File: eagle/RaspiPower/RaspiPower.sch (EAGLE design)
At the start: 6 parts, among them J3 455-1750-1-ND, J4 455-1750-1-ND

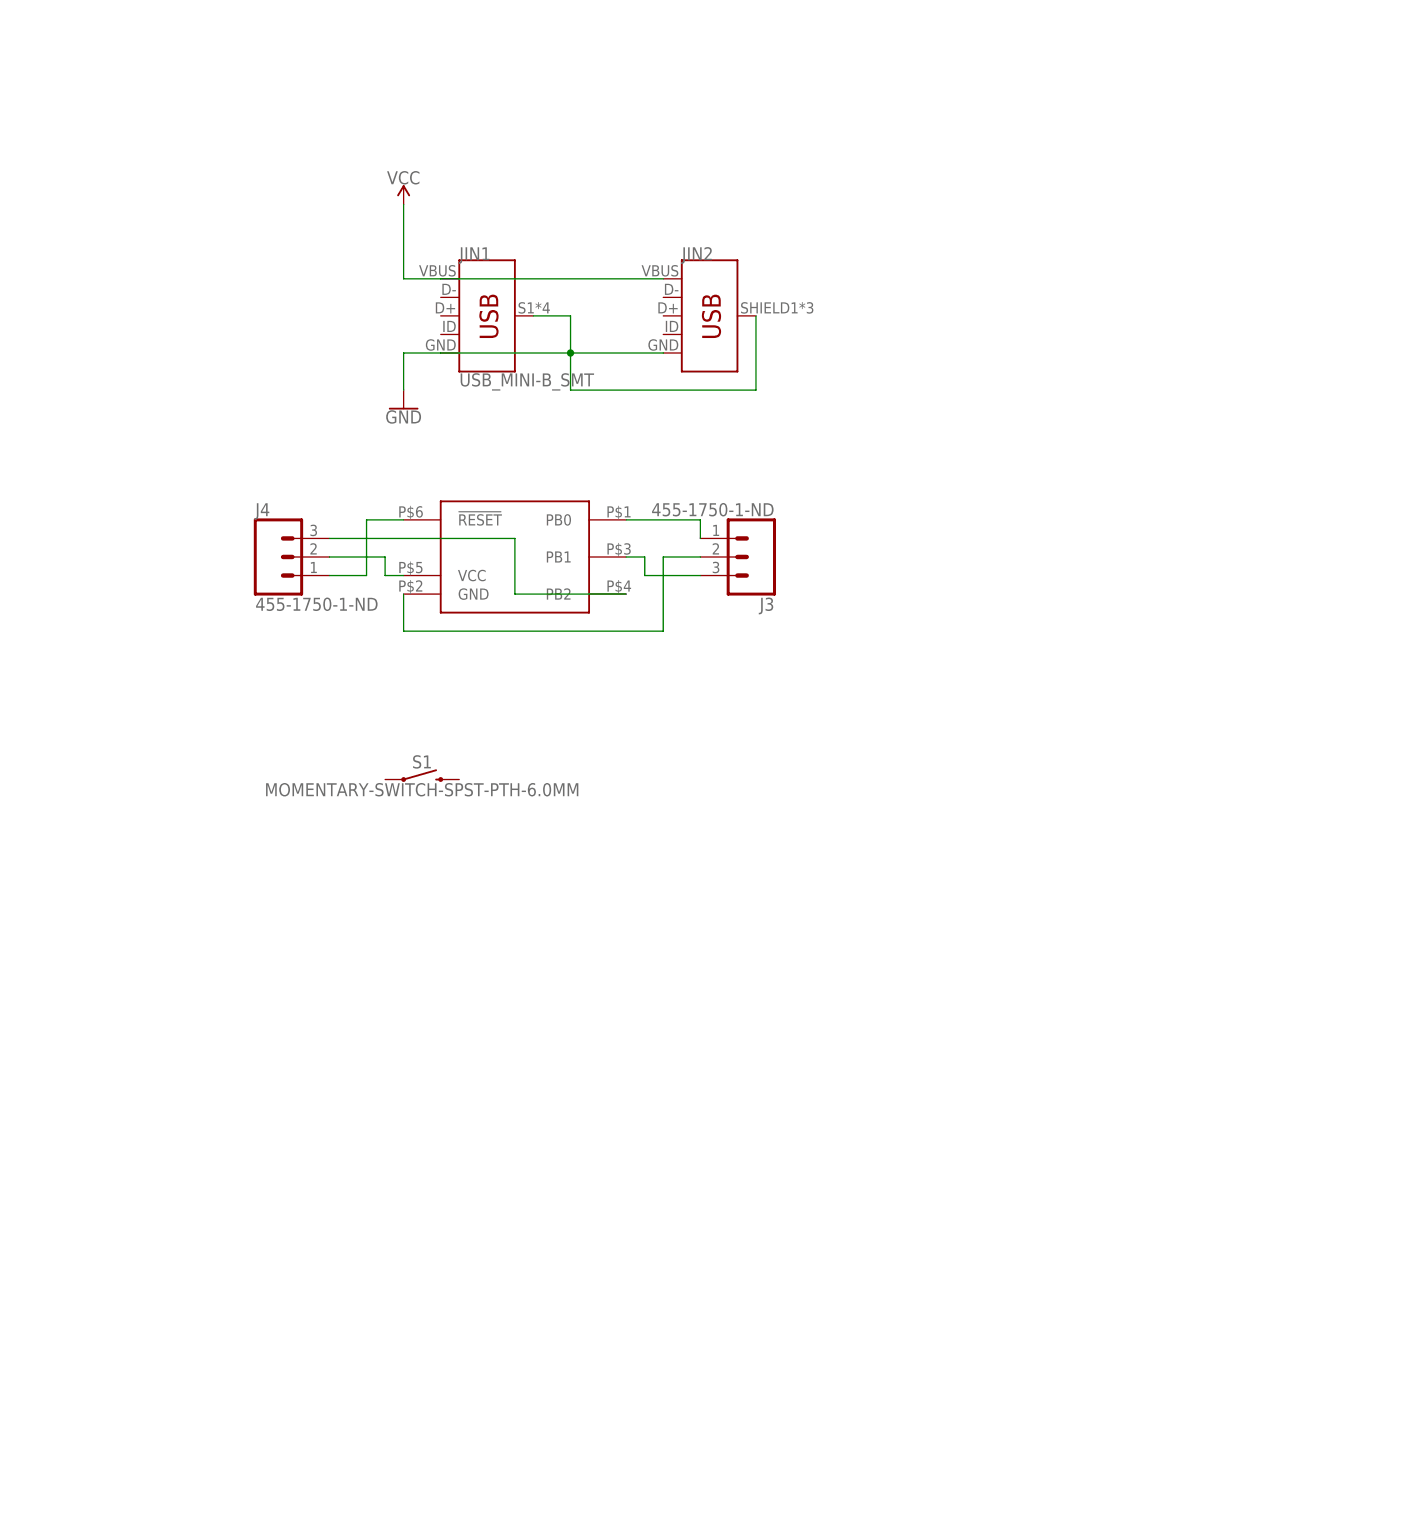
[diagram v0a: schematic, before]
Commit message: edited the Raspipower schematics, some review of components to do before moving to the board design.
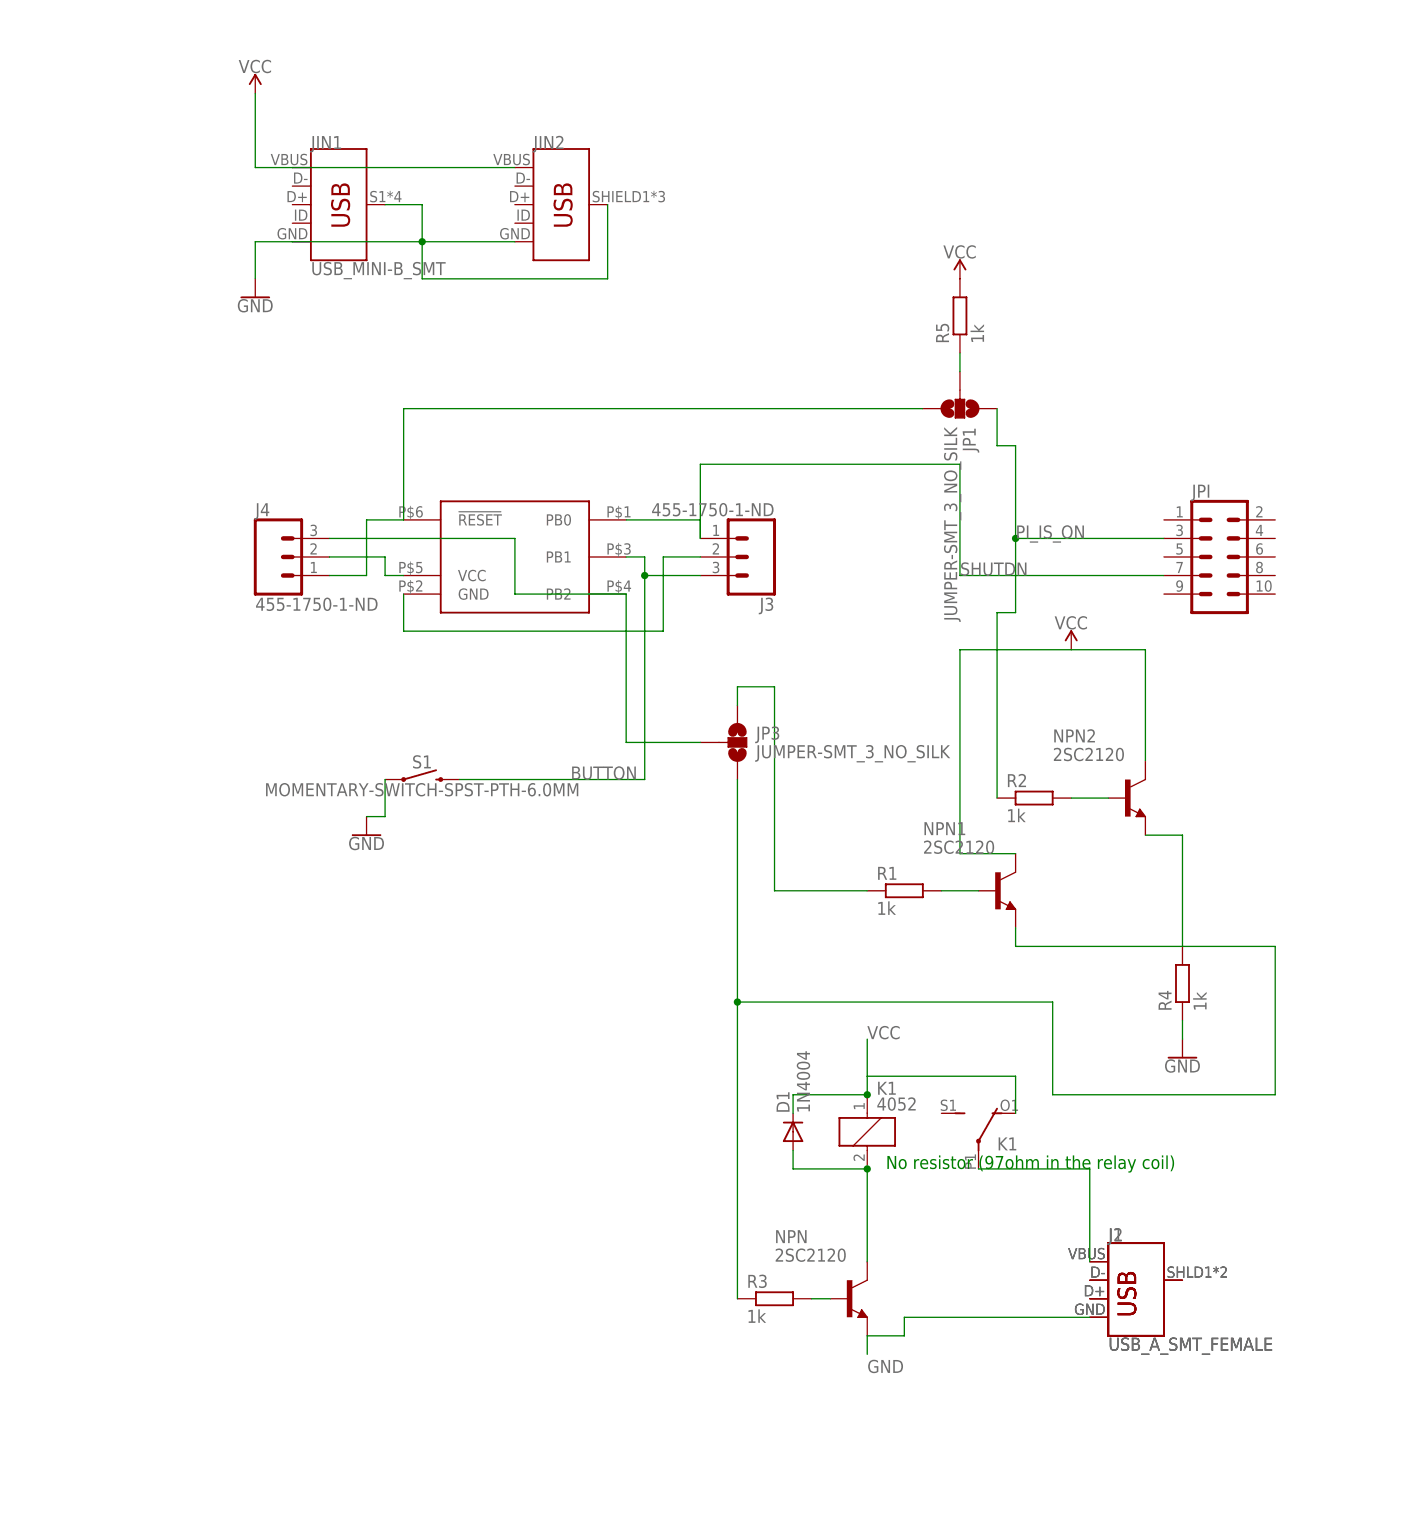
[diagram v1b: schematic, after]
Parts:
- added D1: 1N4004, diode:1N4004
- added J1, J2: USB_A_SMT_FEMALE, SparkFun-Connectors:USB_A_SMT_FEMALE
- added JP1, JP3: JUMPER-SMT_3_NO_SILK, SparkFun-Jumpers:JUMPER-SMT_3_NO_SILK
- added JPI: (no value), SparkFun-Connectors:CONN_05X20.05_IN_PTH_SILK
- added K1: 4052, relay:4052
- added NPN, NPN1, NPN2: 2SC2120, transistor:-NPN-TO92-ECB
- added R1, R2, R3, R4, R5: 1k, resistor:R-EU_0207/2V
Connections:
- new net BUTTON: J3.3, S1.2, U$1.PB1
- new net N$1: J1.D+, J2.D+
- new net N$10: JP1.2, R5.1
- new net N$11: NPN1.B, R1.2
- new net N$12: NPN2.B, R2.2
- new net N$14: JP3.1, R1.1
- new net N$3: J1.VBUS, J2.VBUS, K12.P
- new net N$6: J1.SHIELD, J2.SHIELD
- new net N$8: NPN.B, R3.2
- new net N$9: D1.A, K11.2, NPN.C
- new net PI_IS_ON: JP1.1, JPI.3, R2.1
- new net SHUTDN: J3.1, JPI.7, U$1.PB0
- net GND: now also J1.GND, J2.GND, NPN.E, R4.1, S1.1
- net N$2: now also J1.D-, J2.D-; no longer J3.1, U$1.PB0
- net N$4: now also JP3.3, NPN1.E, NPN2.E, R3.1, R4.2; no longer J3.3, U$1.PB1
- net N$5: now also JP3.2
- net N$7: now also JP1.3
- net VCC: now also D1.C, K11.1, K12.O, NPN1.C, NPN2.C, R5.2
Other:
- note added: "No resistor (97ohm in the relay coil)"
- moved on the sheet: JIN1, JIN2

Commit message: Draft placement, now on to the routing
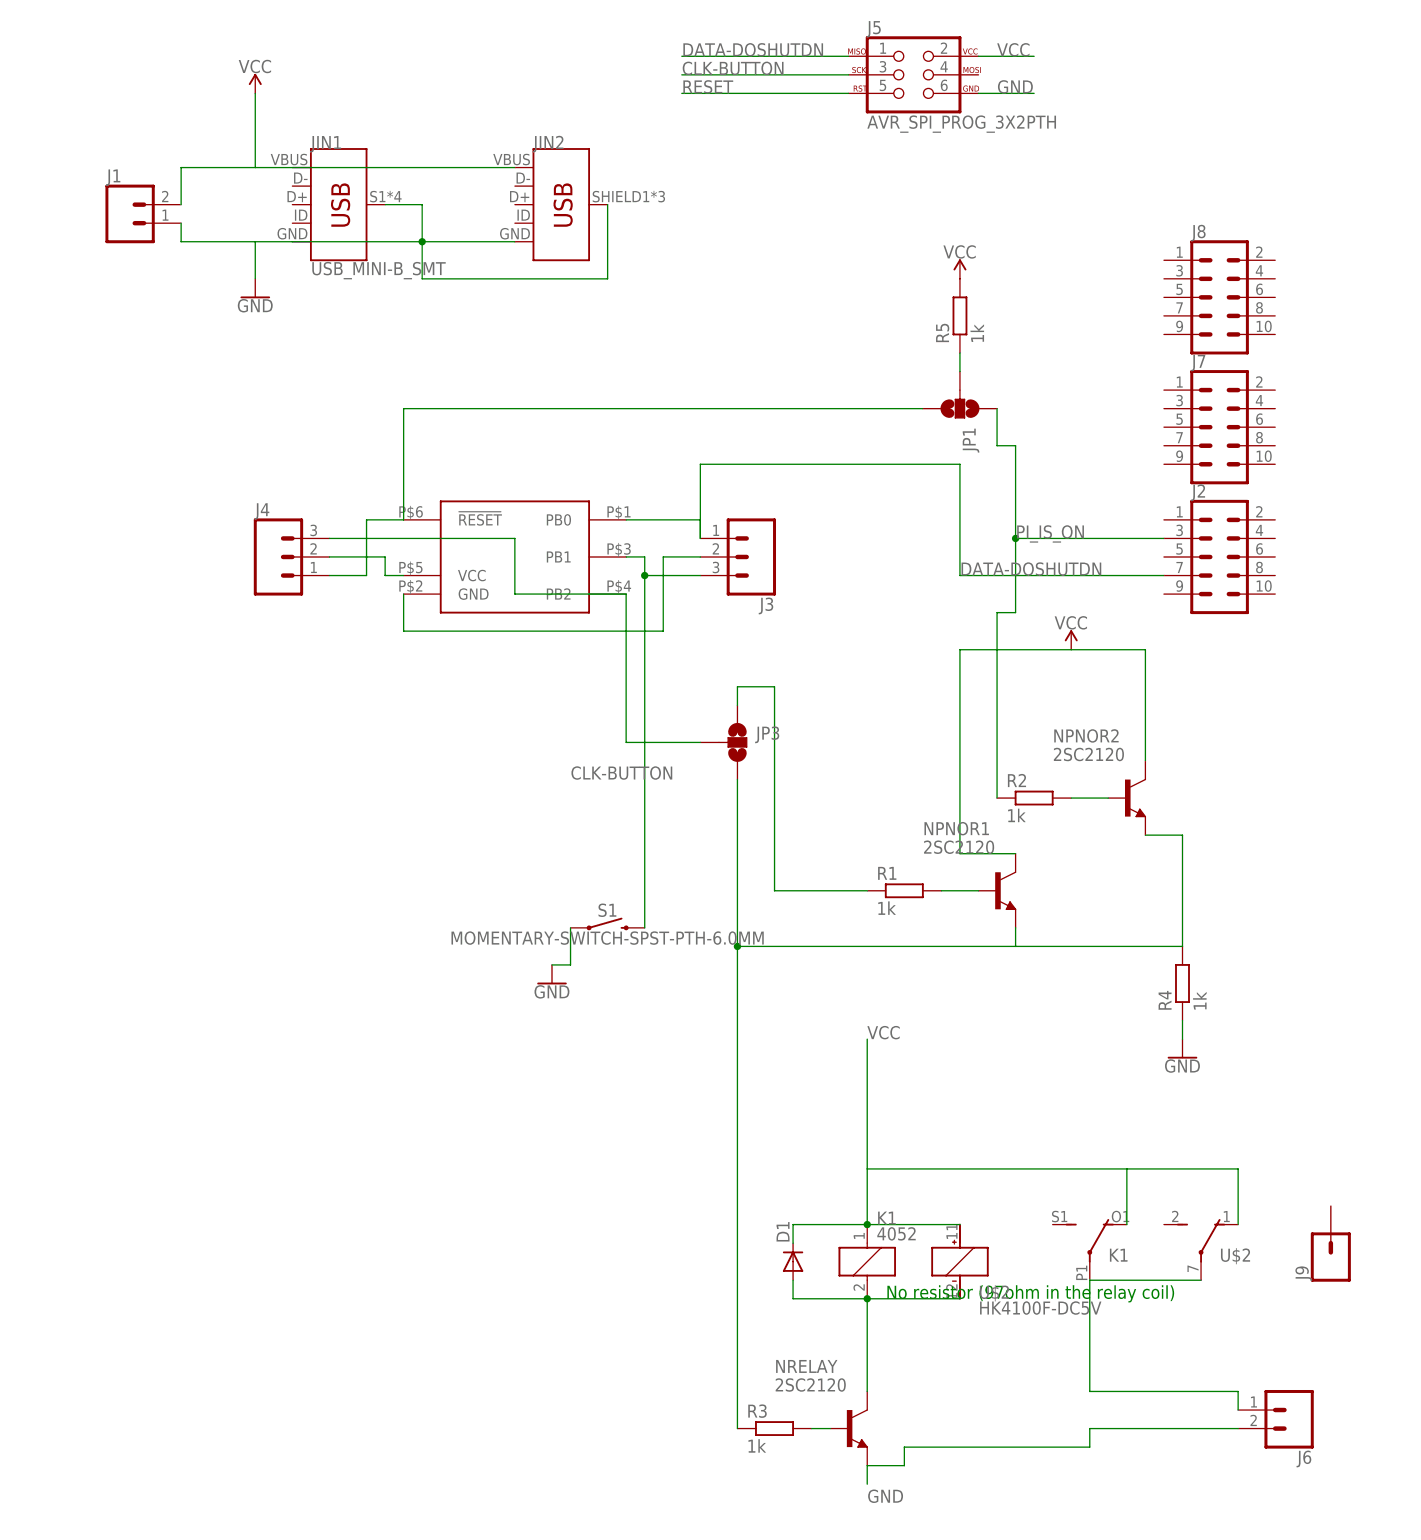
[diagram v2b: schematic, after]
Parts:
- removed JPI: (no value), SparkFun-Connectors:CONN_05X20.05_IN_PTH_SILK
- removed NPN: 2SC2120, transistor:-NPN-TO92-ECB
- added J5: AVR_SPI_PROG_3X2PTH, SparkFun-Connectors:AVR_SPI_PROG_3X2PTH
- added J6: (no value), SparkFun-Connectors:CONN_02LOCK_LONGPADS
- added J7, J8: (no value), SparkFun-Connectors:CONN_05X2PTH
- added J9: (no value), SparkFun-Connectors:CONN_01PTH_NO_SILK_YES_STOP
- added NRELAY: 2SC2120, transistor:-NPN-TO92-ECB
- added U$2: HK4100F-DC5V, huike:HK4100F-DC5V
- D1: value 1N4004 -> (none); device diode:1N4004 -> diode:DIODE-D-2.5
- J1: value USB_A_SMT_FEMALE -> (none); device SparkFun-Connectors:USB_A_SMT_FEMALE -> SparkFun-Connectors:CONN_02LOCK_LONGPADS
- J2: value USB_A_SMT_FEMALE -> (none); device SparkFun-Connectors:USB_A_SMT_FEMALE -> SparkFun-Connectors:CONN_05X2PTH
- J3, J4: value 455-1750-1-ND -> (none)
- R3: device resistor:R-EU_0207/2V -> resistor:R-EU_0204/7
- renumbered NPN1 to NPNOR1, NPN2 to NPNOR2
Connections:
- removed net BUTTON: J3.3, S1.2, U$1.PB1
- removed net N$1: J1.D+, J2.D+
- removed net N$2: J1.D-, J2.D-
- removed net N$6: J1.SHIELD, J2.SHIELD
- removed net N$7: J4.1, JP1.3, U$1.!RESET
- removed net SHUTDN: J3.1, JPI.7, U$1.PB0
- new net CLK-BUTTON: J3.3, J5.3, S1.2, U$1.PB1
- new net DATA-DOSHUTDN: J2.7, J3.1, J5.1, U$1.PB0
- new net RESET: J4.1, J5.5, JP1.3, U$1.!RESET
- net GND: now also J1.1, J5.6, J6.2, NRELAY.E; no longer J1.GND, J2.GND, NPN.E
- net N$3: now also J6.1, U$2G$2.P; no longer J1.VBUS, J2.VBUS
- net N$8: now also NRELAY.B; no longer NPN.B
- net N$9: now also NRELAY.C, U$2G$1.-; no longer NPN.C
- net PI_IS_ON: now also J2.3; no longer JPI.3
- net VCC: now also J1.2, J5.2, U$2G$1.+, U$2G$2.O
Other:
- moved on the sheet: K1, R3, S1
